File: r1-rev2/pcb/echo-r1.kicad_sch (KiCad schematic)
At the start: 100 parts, among them J1 TYPE-C-31-M-12, J2 TF-115, J6 AFC07-S30ECA-00, J7 Conn_01x04, J8 Conn_01x05, Q1 AO3401A, Q2 AO3401A, SW1 A, SW10 SELECT, SW11 VOL+, SW12 VOL-, SW13 POWER, SW14 HOLD, SW2 B, SW3 X, SW4 Y, SW5 DPAD↑, SW6 DPAD↓, SW7 DPAD←, SW8 DPAD→, SW9 START, U1 STM32H7R3Z8Jx, U10 USBLC6-2SC6, U11 TPAZ1143-04F, U12 TPAZ1143-04F, U13 TPAZ1143-04F, U14 TPAZ1143-04F, U2 W958D8NBYA5I, Y1 SC-32S32.768kHz20PPM12.5pF, Y2 XTM32024000JT00351001

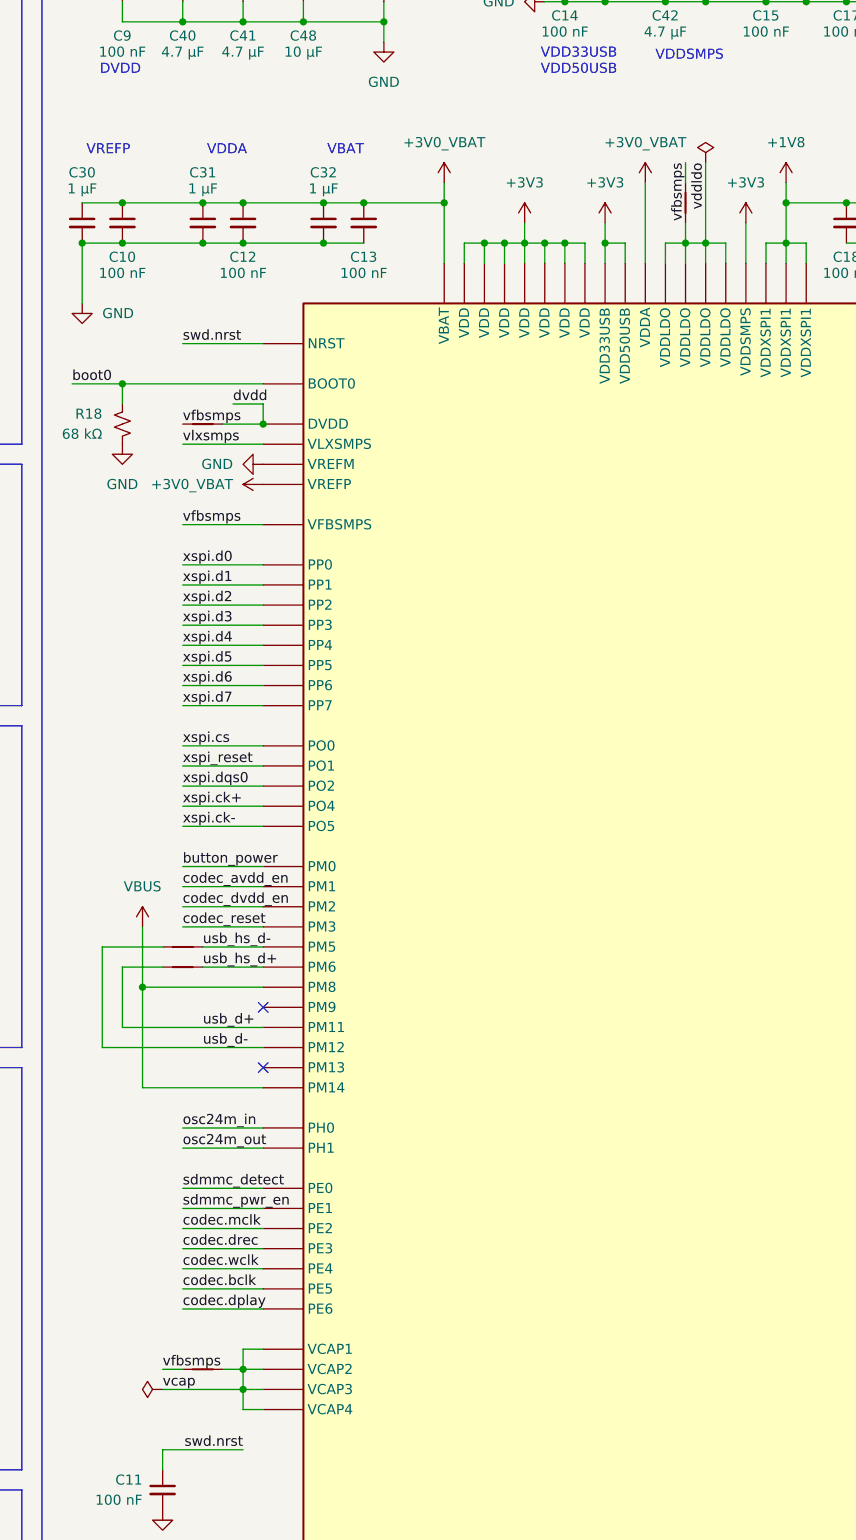
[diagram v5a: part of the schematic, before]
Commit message: R1-Rev2: WIP STM32 crystal and SMPS layout
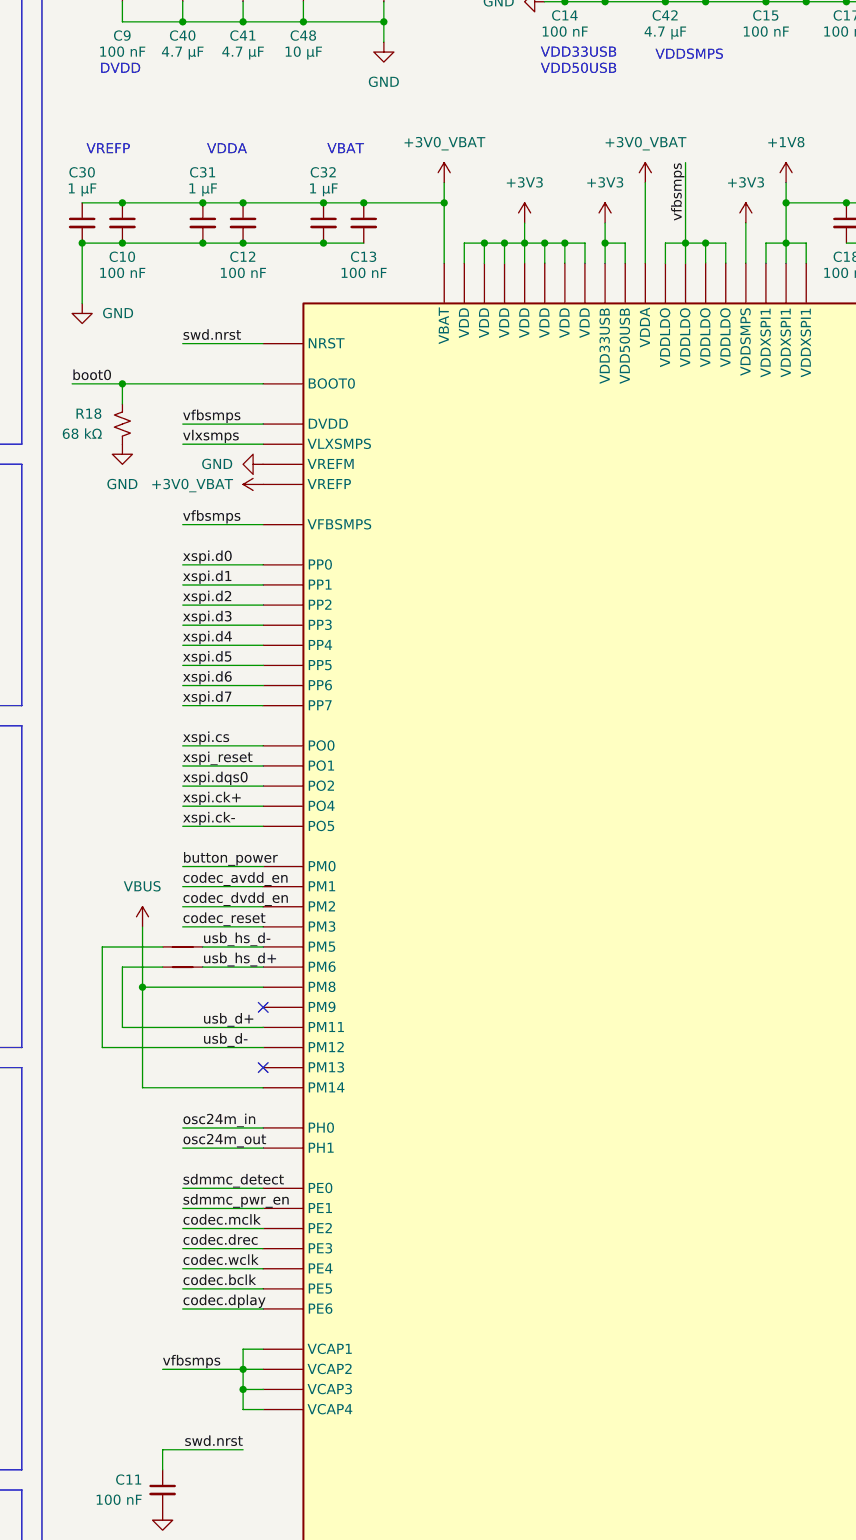
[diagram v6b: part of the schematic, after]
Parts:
- removed NT10, NT4, NT5: NetTie_2, echoplayer:NetTie_0.15mm_SMD, symbol Device:NetTie_2
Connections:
- net dvdd is gone; now on net vfbsmps: U1.C8 (DVDD)
- net vcap is gone; now on net vfbsmps: U1.E5 (VCAP4), U1.F8 (VCAP3), U1.H6 (VCAP1), U1.H8 (VCAP2)
- net vddldo is gone; now on net vfbsmps: U1.F6 (VDDLDO), U1.F7 (VDDLDO), U1.G6 (VDDLDO), U1.G7 (VDDLDO)

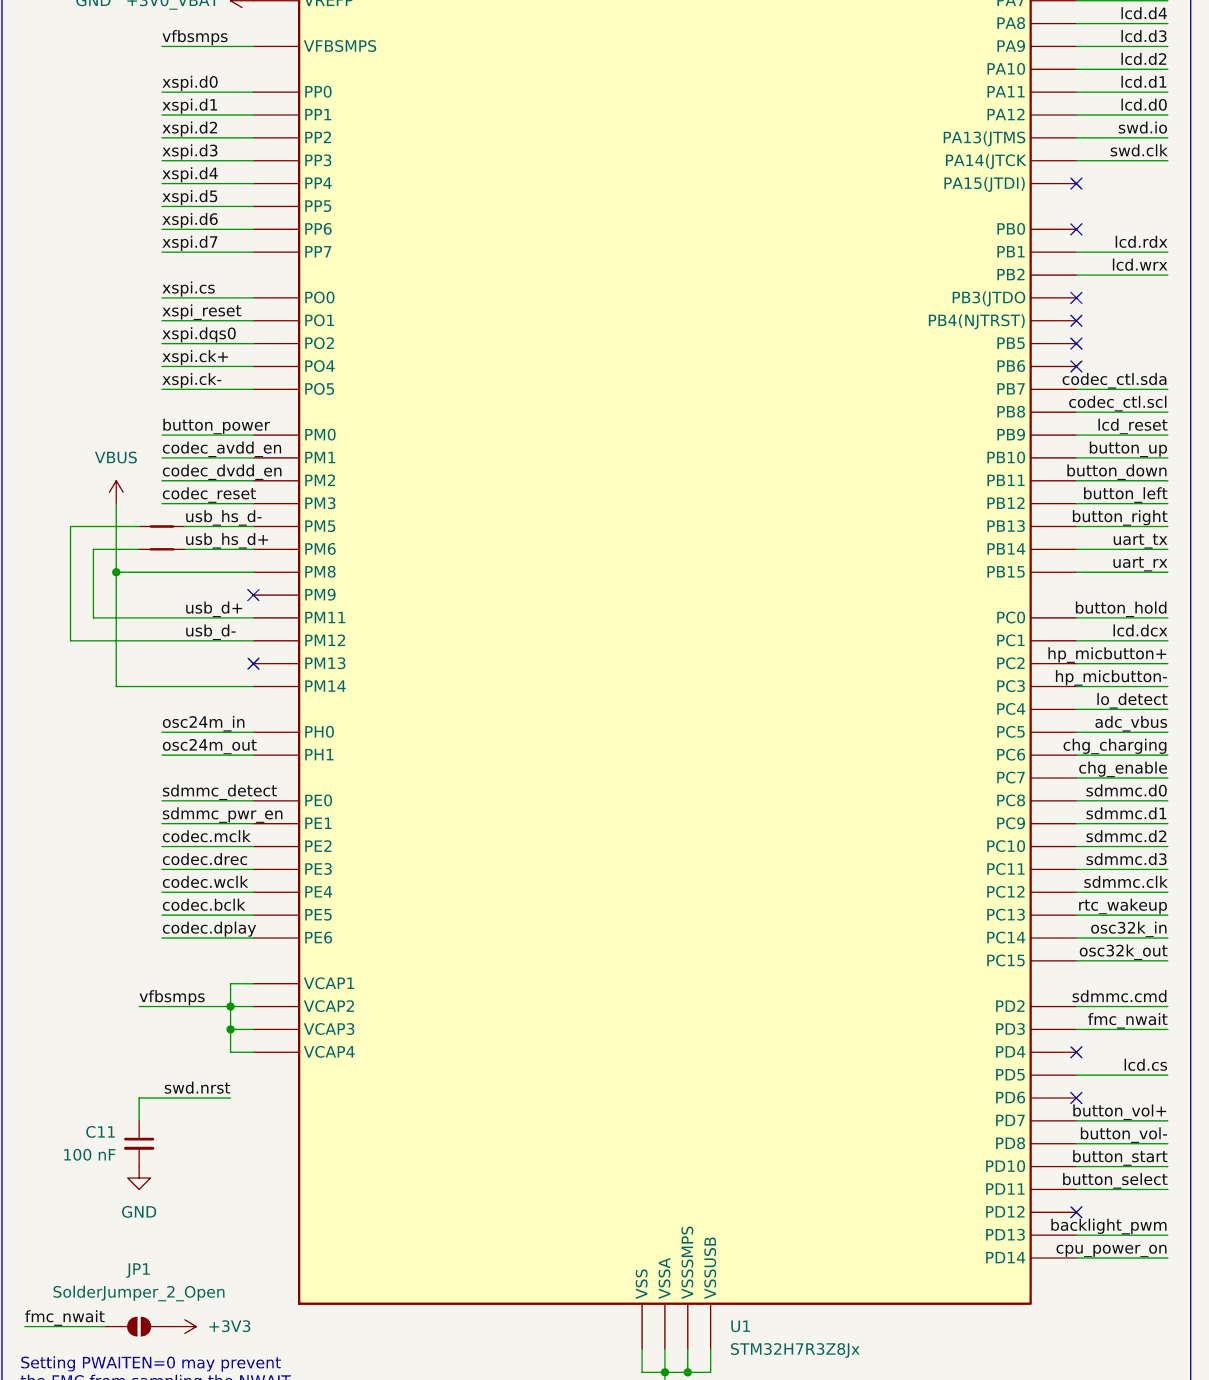
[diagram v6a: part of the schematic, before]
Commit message: R1-Rev2: WIP STM32 signal and power routing
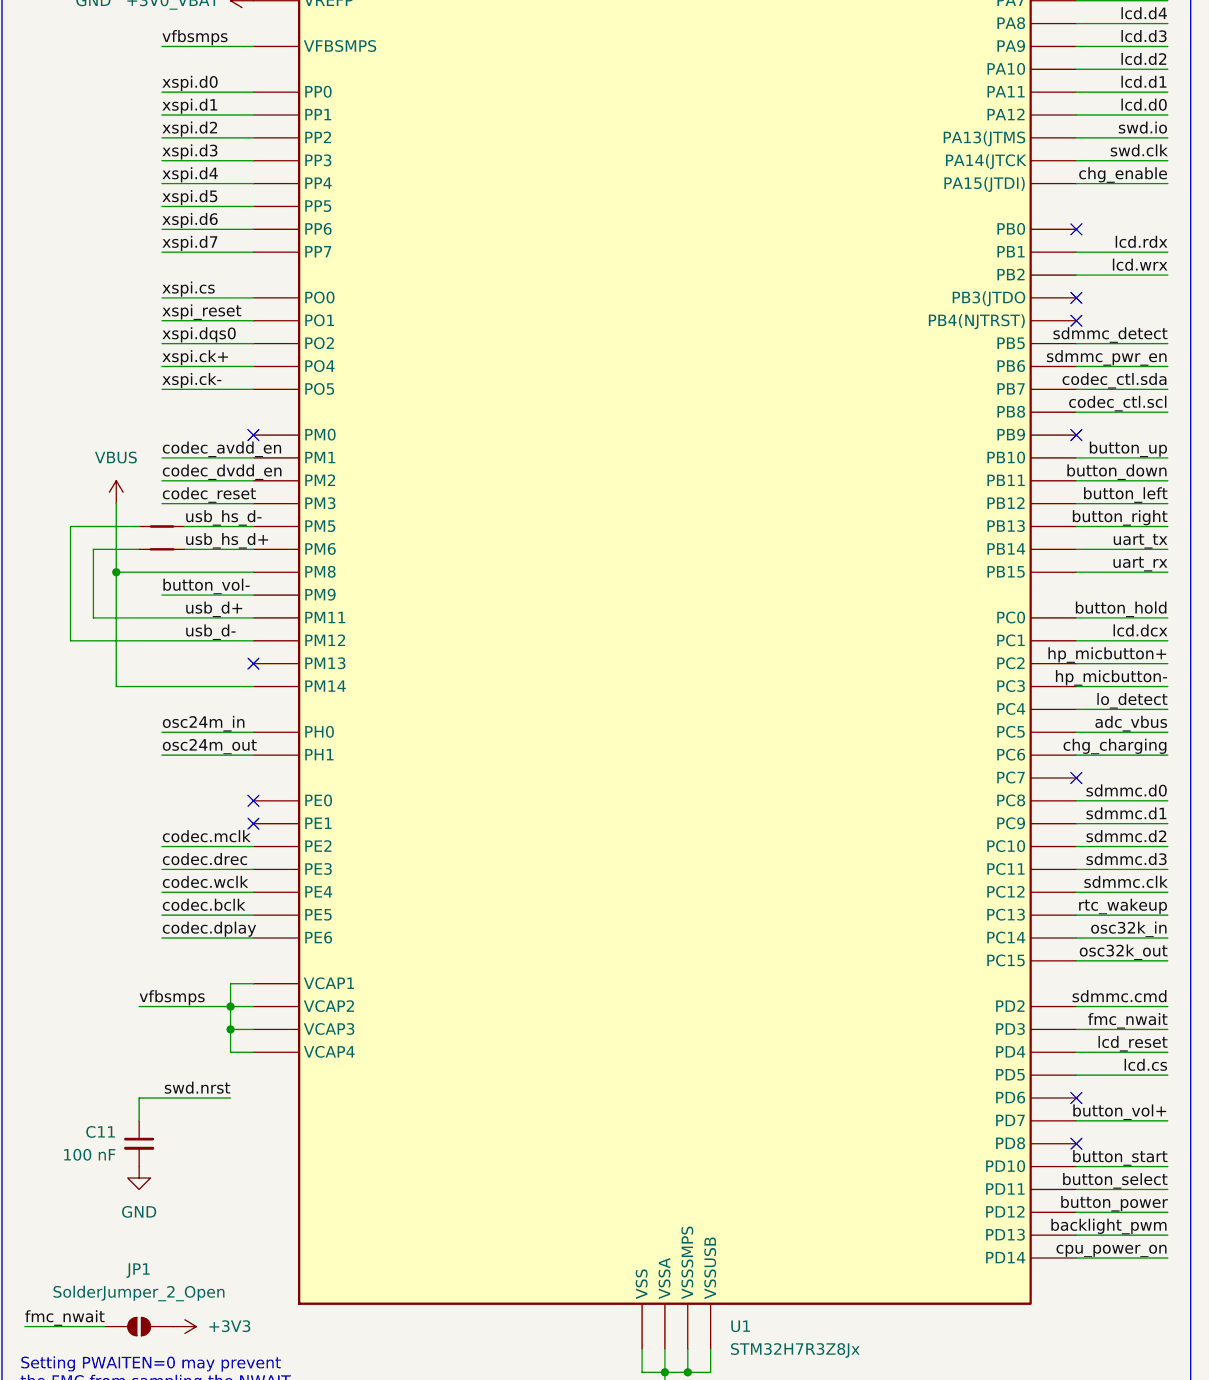
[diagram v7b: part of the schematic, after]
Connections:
- net button_power: now also U1.K11 (PD12); no longer U1.E8 (PM0)
- net button_vol-: now also U1.A8 (PM9); no longer U1.J8 (PD8)
- net chg_enable: now also U1.D12 (PA15(JTDI)); no longer U1.G9 (PC7)
- net lcd_reset: now also U1.B12 (PD4); no longer U1.C3 (PB9)
- net sdmmc_detect: now also U1.A4 (PB5); no longer U1.B4 (PE0)
- net sdmmc_pwr_en: now also U1.A3 (PB6); no longer U1.B3 (PE1)

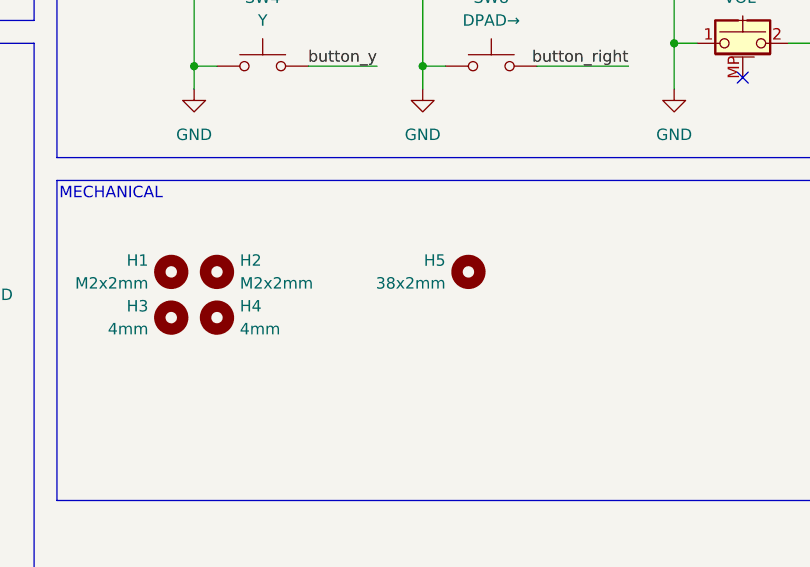
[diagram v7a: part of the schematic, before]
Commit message: R1-Rev2: move LCD in Z-axis to free up board space
Mounting the LCD directly to the PCB just proved to be too
awkward; mainly because the connector position made it hard
to fit components on the upper half of the PCB. Mounting it
on top of a 1.2mm support which directly contacts the PCB
alleviates this, and the cable slot can now be smaller and
moved up closer to the connector. This provides a bit more
room everywhere and will make placement & routing simpler.

There is a slight impact on thickness, but the acrylic LCD
cover can be reduced in thickness to compensate.
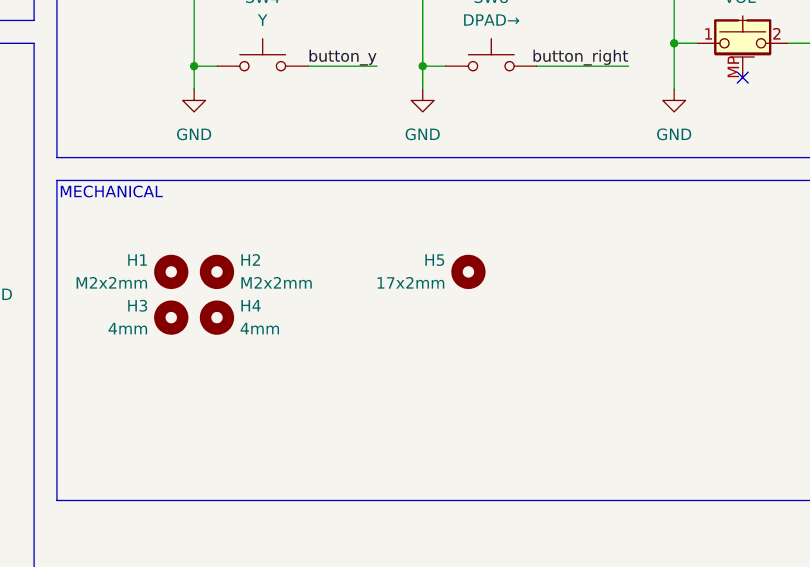
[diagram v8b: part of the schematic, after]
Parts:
- H5: value 38x2mm -> 17x2mm; footprint echoplayer:Slot_38x2mm -> echoplayer:Slot_17x2mm
